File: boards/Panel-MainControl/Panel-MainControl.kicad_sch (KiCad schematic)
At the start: 26 parts, among them J1 ISP, J10 Conn_01x10, J11 Conn_01x10, J2 PanelRight, J3 Volume, J4 Btn1, J5 Btn3, J6 Btn5, J7 Btn2, J8 Btn4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

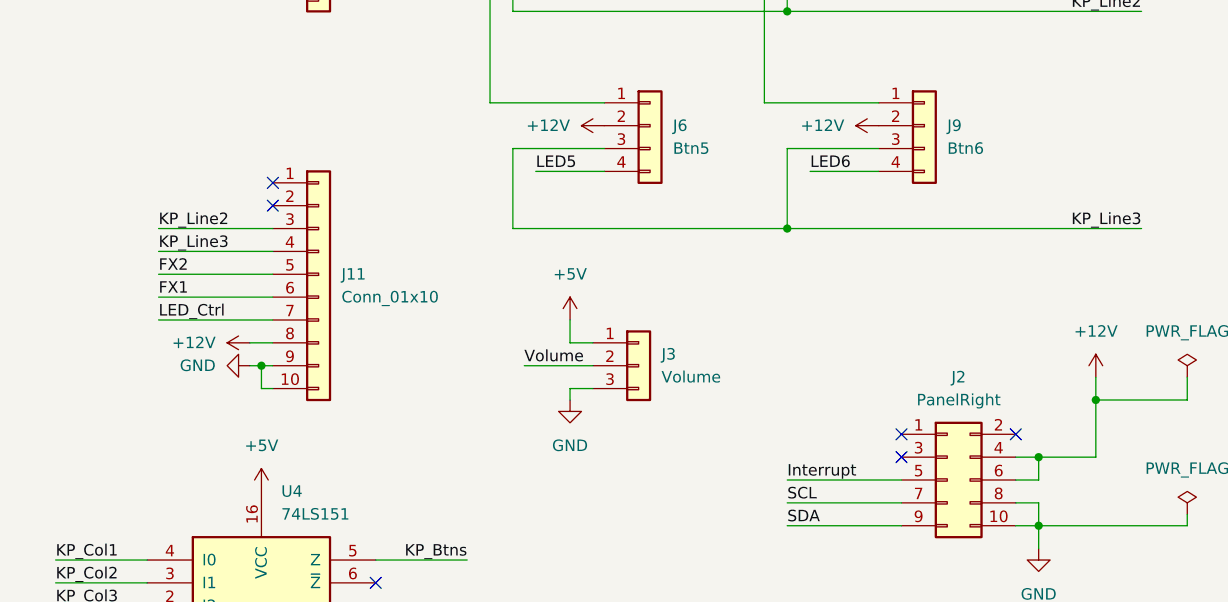
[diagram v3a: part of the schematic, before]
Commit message: Fixed using 5V from main power for PWR LED
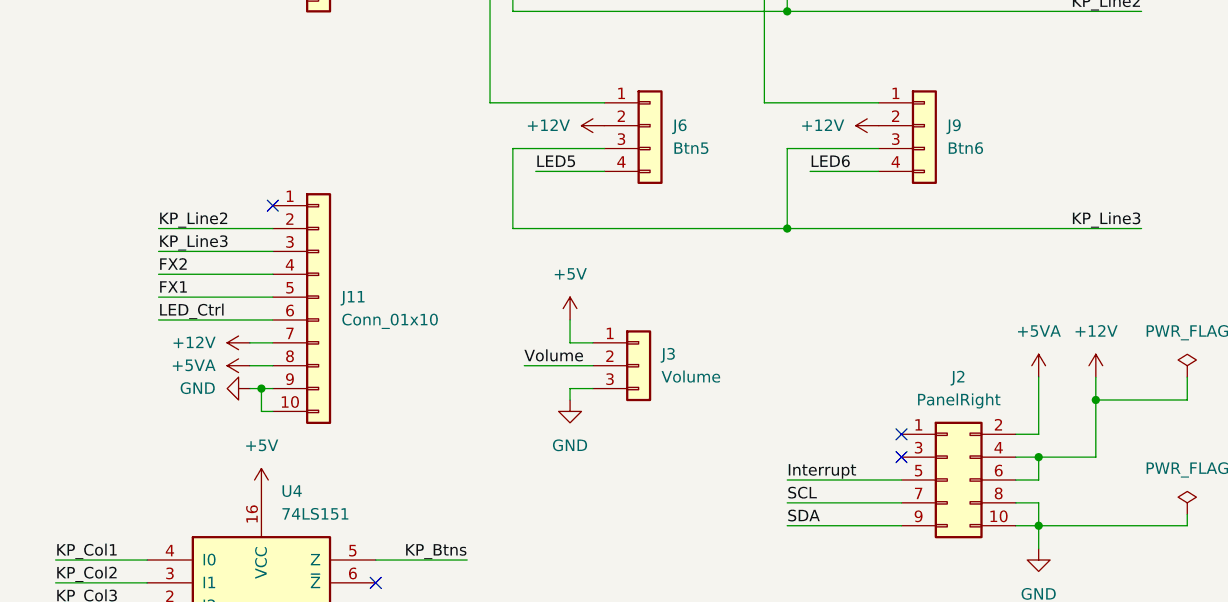
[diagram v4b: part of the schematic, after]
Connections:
- net +12V: now also J11.7 (Pin_7); no longer J11.8 (Pin_8)
- net FX1: now also J11.5 (Pin_5); no longer J11.6 (Pin_6)
- net FX2: now also J11.4 (Pin_4); no longer J11.5 (Pin_5)
- net KP_Line2: now also J11.2 (Pin_2); no longer J11.3 (Pin_3)
- net KP_Line3: now also J11.3 (Pin_3); no longer J11.4 (Pin_4)
- net LED_Ctrl: now also J11.6 (Pin_6); no longer J11.7 (Pin_7)
- net +5VA: now reaches J2.2 (Pin_2)
- net +5VA: now also J11.8 (Pin_8)
- no-connect marks 10 -> 8
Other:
- moved on the sheet: J11
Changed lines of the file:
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@@
 	)
 	(junction
-		(at 157.48 121.92)
+		(at 157.48 124.46)
 		(diameter 0)
 		(color 0 0 0 0)
@@
 	)
 	(no_connect
-		(at 241.3 129.54)
-	)
-	(no_connect
-		(at 158.75 101.6)
-	)
-	(no_connect
 		(at 97.79 36.83)
 	)
@@
 	(wire
 		(pts
-			(xy 157.48 121.92) (xy 156.21 121.92)
+			(xy 157.48 124.46) (xy 156.21 124.46)
 		)
 		(stroke
@@
 	(wire
 		(pts
-			(xy 157.48 124.46) (xy 157.48 121.92)
+			(xy 157.48 127) (xy 157.48 124.46)
 		)
 		(stroke
@@
 	(wire
 		(pts
+			(xy 243.84 129.54) (xy 241.3 129.54)
+		)
+		(stroke
+			(width 0)
+			(type default)
+		)
+	)
+	(wire
+		(pts
 			(xy 142.24 176.53) (xy 144.78 176.53)
 		)
@@
 	(wire
 		(pts
+			(xy 243.84 123.19) (xy 243.84 129.54)
+		)
+		(stroke
+			(width 0)
+			(type default)
+		)
+	)
+	(wire
+		(pts
 			(xy 146.05 81.28) (xy 158.75 81.28)
 		)
@@
 	(wire
 		(pts
-			(xy 158.75 121.92) (xy 157.48 121.92)
+			(xy 158.75 124.46) (xy 157.48 124.46)
 		)
 		(stroke
@@
 	(wire
 		(pts
+			(xy 156.21 121.92) (xy 158.75 121.92)
+		)
+		(stroke
+			(width 0)
+			(type default)
+		)
+	)
+	(wire
+		(pts
 			(xy 156.21 58.42) (xy 156.21 55.88)
 		)
@@
 	(wire
 		(pts
-			(xy 158.75 124.46) (xy 157.48 124.46)
+			(xy 158.75 127) (xy 157.48 127)
 		)
 		(stroke
@@
 	(symbol
 		(lib_id "Connector_Generic:Conn_01x10")
-		(at 163.83 111.76 0)
+		(at 163.83 114.3 0)
 		(unit 1)
 		(exclude_from_sim no)
@@
 		(fields_autoplaced yes)
 		(property "Reference" "J11"
-			(at 166.37 111.7599 0)
+			(at 166.37 114.2999 0)
 			(effects
 				(font
@@
 		)
 		(property "Value" "Conn_01x10"
-			(at 166.37 114.2999 0)
+			(at 166.37 116.8399 0)
 			(effects
 				(font
@@
 		)
 		(property "Footprint" "Connector_PinHeader_2.00mm:PinHeader_1x10_P2.00mm_Vertical"
-			(at 163.83 111.76 0)
+			(at 163.83 114.3 0)
 			(effects
 				(font
@@
 		)
 		(property "Datasheet" "~"
-			(at 163.83 111.76 0)
+			(at 163.83 114.3 0)
 			(effects
 				(font
@@
 		)
 		(property "Description" "Generic connector, single row, 01x10, script generated (kicad-library-utils/schlib/autogen/connector/)"
-			(at 163.83 111.76 0)
+			(at 163.83 114.3 0)
 			(effects
 				(font
@@
 	(symbol
 		(lib_id "power:GND")
-		(at 156.21 121.92 270)
+		(at 156.21 124.46 270)
 		(unit 1)
 		(exclude_from_sim no)
@@
 		(fields_autoplaced yes)
 		(property "Reference" "#PWR032"
-			(at 149.86 121.92 0)
+			(at 149.86 124.46 0)
 			(effects
 				(font
@@
 		)
 		(property "Value" "GND"
-			(at 152.4 121.9199 90)
+			(at 152.4 124.4599 90)
 			(effects
 				(font
@@
 		)
 		(property "Footprint" ""
-			(at 156.21 121.92 0)
+			(at 156.21 124.46 0)
 			(effects
 				(font
@@
 		)
 		(property "Datasheet" ""
-			(at 156.21 121.92 0)
+			(at 156.21 124.46 0)
 			(effects
 				(font
@@
 		)
 		(property "Description" "Power symbol creates a global label with name \"GND\" , ground"
-			(at 156.21 121.92 0)
+			(at 156.21 124.46 0)
 			(effects
 				(font
@@
 					(unit 1)
 				)
+			)
+		)
+	)
+	(symbol
+		(lib_id "power:+5VA")
+		(at 243.84 123.19 0)
+		(unit 1)
+		(exclude_from_sim no)
+		(in_bom yes)
+		(on_board yes)
+		(dnp no)
+		(fields_autoplaced yes)
+		(property "Reference" "#PWR029"
+			(at 243.84 127 0)
+			(effects
+				(font
+					(size 1.27 1.27)
+				)
+				(hide yes)
+			)
+		)
+		(property "Value" "+5VA"
+			(at 243.84 118.11 0)
+			(effects
+				(font
+					(size 1.27 1.27)
+				)
+			)
+		)
+		(property "Footprint" ""
+			(at 243.84 123.19 0)
+			(effects
+				(font
+					(size 1.27 1.27)
+				)
+				(hide yes)
+			)
+		)
+		(property "Datasheet" ""
+			(at 243.84 123.19 0)
+			(effects
+				(font
+					(size 1.27 1.27)
+				)
+				(hide yes)
+			)
+		)
+		(property "Description" "Power symbol creates a global label with name \"+5VA\""
+			(at 243.84 123.19 0)
+			(effects
+				(font
+					(size 1.27 1.27)
+				)
+				(hide yes)
+			)
+		)
+		(pin "1"
+		)
+		(instances
+			(project ""
+				(path "/2777062a-260a-49c7-9a79-289c63518b5f"
+					(reference "#PWR029")
+					(unit 1)
+				)
+			)
+		)
+	)
+	(symbol
+		(lib_id "power:+5VA")
+		(at 156.21 121.92 90)
+		(unit 1)
+		(exclude_from_sim no)
+		(in_bom yes)
+		(on_board yes)
+		(dnp no)
+		(fields_autoplaced yes)
+		(property "Reference" "#PWR030"
+			(at 160.02 121.92 0)
+			(effects
+				(font
+					(size 1.27 1.27)
+				)
+				(hide yes)
+			)
+		)
+		(property "Value" "+5VA"
+			(at 152.4 121.9199 90)
+			(effects
+				(font
+					(size 1.27 1.27)
+				)
+				(justify left)
+			)
+		)
+		(property "Footprint" ""
+			(at 156.21 121.92 0)
+			(effects
+				(font
+					(size 1.27 1.27)
+				)
+				(hide yes)
+			)
+		)
+		(property "Datasheet" ""
+			(at 156.21 121.92 0)
+			(effects
+				(font
+					(size 1.27 1.27)
+				)
+				(hide yes)
+			)
+		)
+		(property "Description" "Power symbol creates a global label with name \"+5VA\""
+			(at 156.21 121.92 0)
+			(effects
+				(font
+					(size 1.27 1.27)
+				)
+				(hide yes)
+			)
+		)
+		(pin "1"
+		)
+		(instances
+			(project "Panel-MainControl"
+				(path "/2777062a-260a-49c7-9a79-289c63518b5f"
+					(reference "#PWR030")
+					(unit 1)
+				)

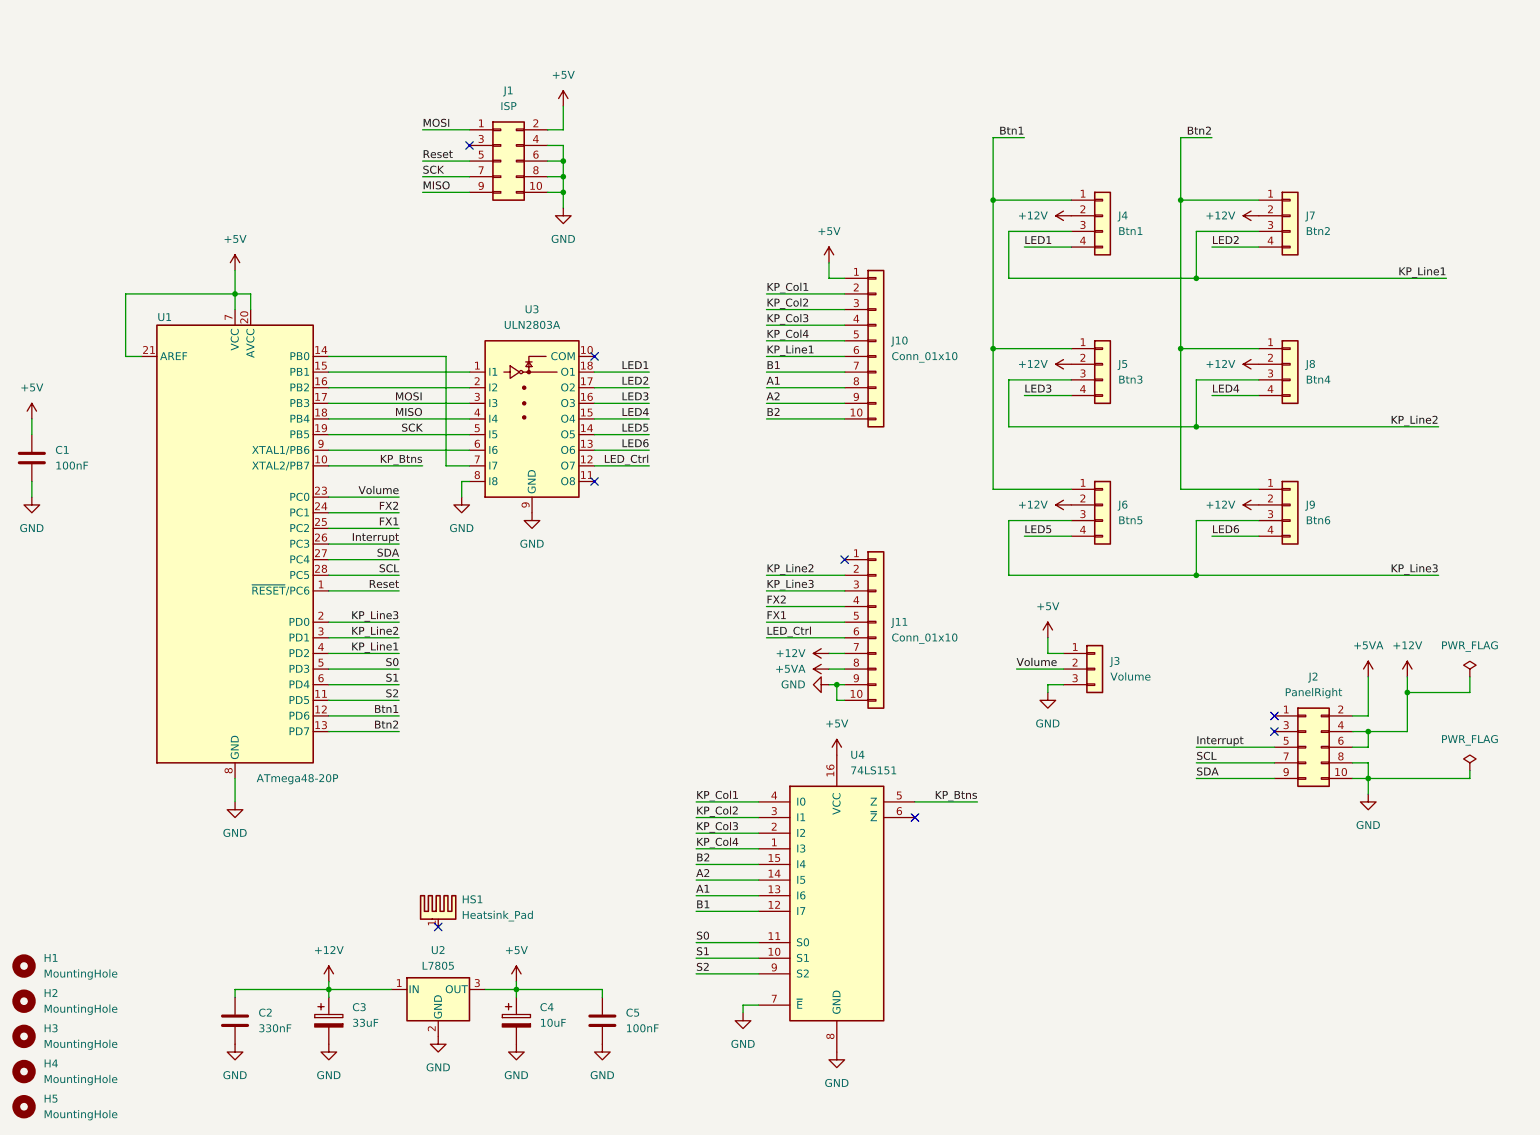
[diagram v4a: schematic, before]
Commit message: Fixes for missing pullups on keypad buttons
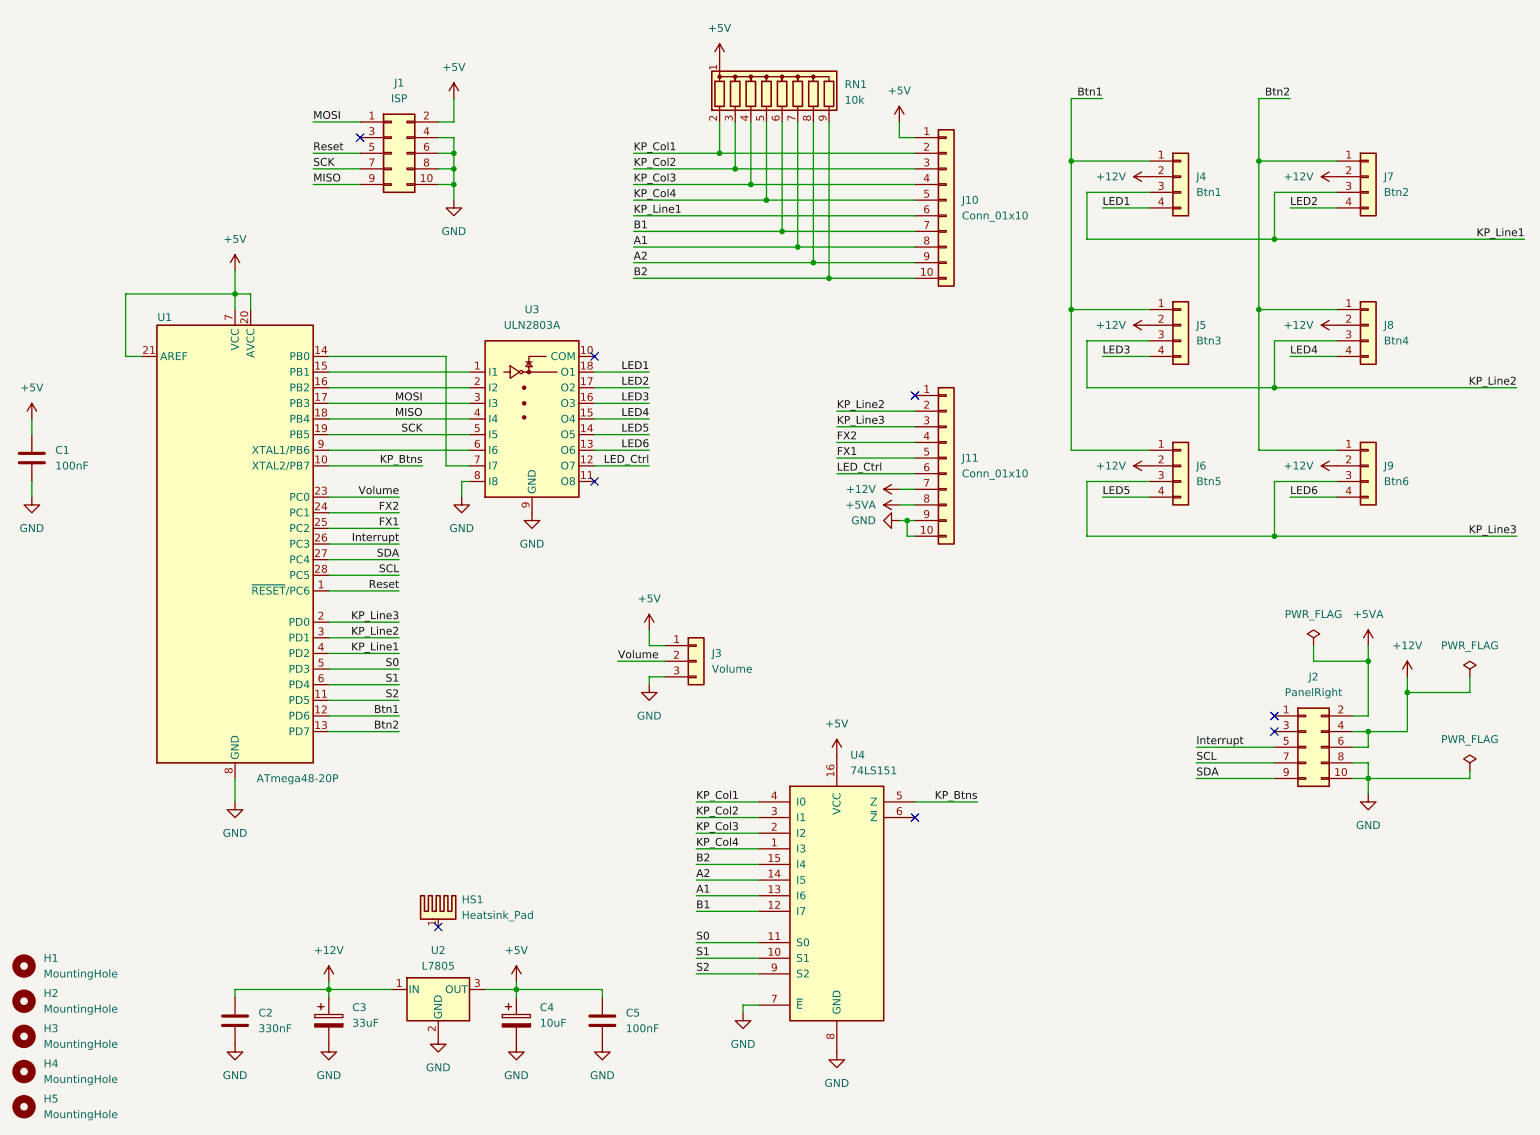
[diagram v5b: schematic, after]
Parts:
- added RN1: 10k, Resistor_THT:R_Array_SIP9, symbol Device:R_Network08
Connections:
- net +5V: now also RN1.1 (common)
- net A1: now also RN1.7 (R6)
- net A2: now also RN1.8 (R7)
- net B1: now also RN1.6 (R5)
- net B2: now also RN1.9 (R8)
- net KP_Col1: now also RN1.2 (R1)
- net KP_Col2: now also RN1.3 (R2)
- net KP_Col3: now also RN1.4 (R3)
- net KP_Col4: now also RN1.5 (R4)
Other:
- moved on the sheet: J1, J10, J11, J3, J4, J5, J6, J7, J8, J9
